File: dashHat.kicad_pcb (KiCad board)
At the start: 4 copper layers, 65 x 56 mm, 156 parts, among them J1 Input, J2 LCD, J3 GPIO, J4 LEDs, J5 Ride Through, J6 SMA, J7 Conn_01x08, Q1 BSS138, Q10 ADP197, Q12 BSS138, Q2 BSS138, Q3 2N7002, Q4 BSS84, Q5 BSS84, Q6 BSS84, Q7 , Q8 , Q9 BSS84, U1 CAT24C256, U12 MAX22193, U13 IX4427, U2 MAX17614, U3 TVS3300DRV, U4 LM61480, U5 74LVC1G80, U6 ZOE-M8Q, U7 TCAN330, U8 MCP2515-xST, U9 MAX3227, Y1 32.768k, Y2 12MHz

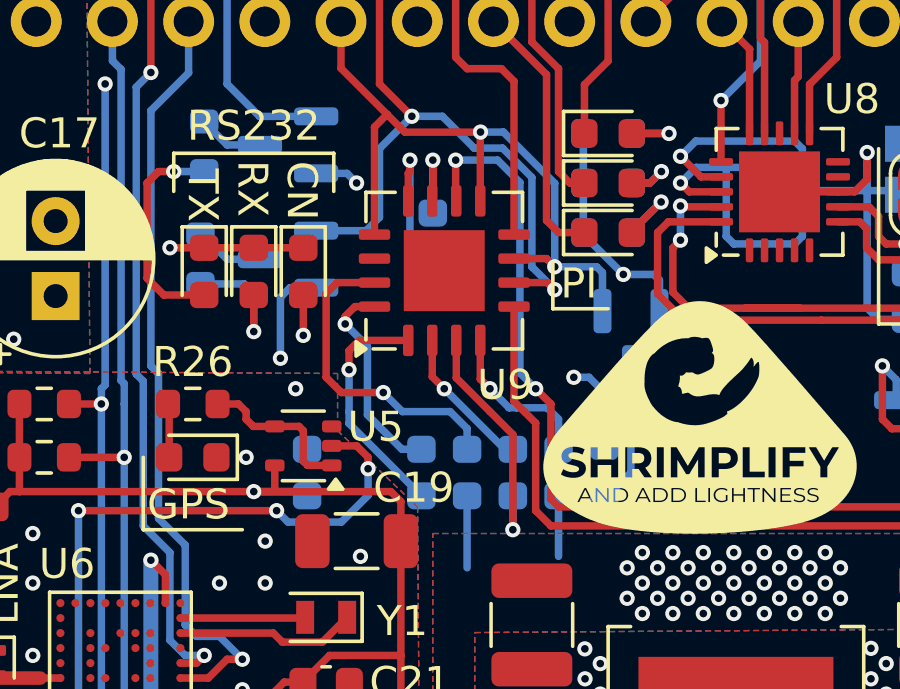
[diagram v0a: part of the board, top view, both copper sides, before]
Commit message: flip logic on rs232 conn led
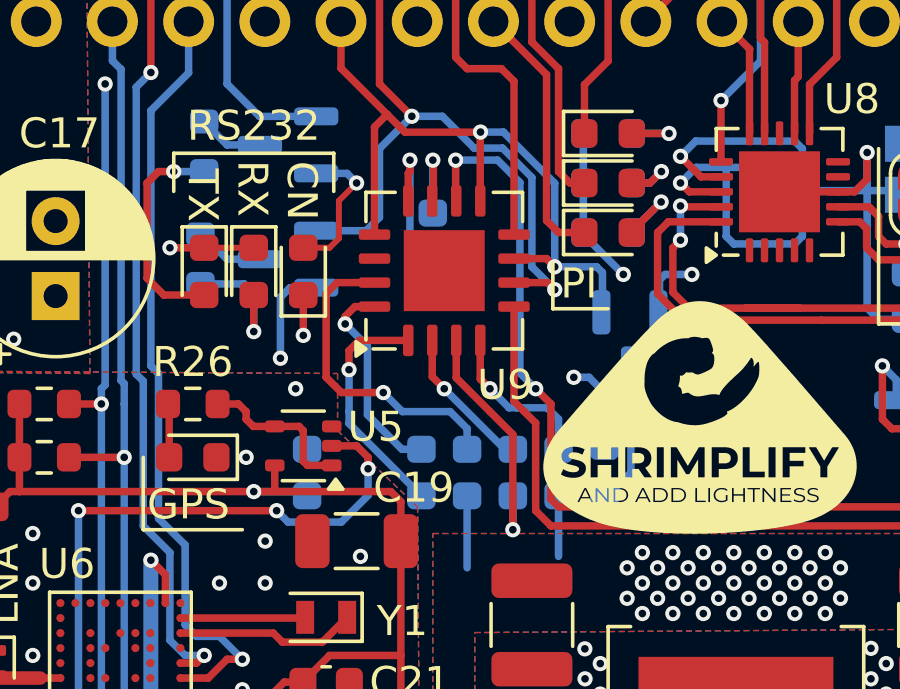
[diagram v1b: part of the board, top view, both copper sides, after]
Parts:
- Q6: value BSS84 -> 2N7002
- R1, R3: value 1.8k -> 1.5k
- R19: value 560 -> 680
- R25, R27, R28, R5, R6: value 3.9k -> 3.3k
- R26, R31, R32, R33, R34, R43, R46, R47, R7: value 220 -> 270
- moved Q6 0.05 mm to (130.7, 59.4)
- turned D13 to 90 degrees
- turned R34 to -90 degrees
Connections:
- D13 pad 1: GND -> Net-(D13-K)
- D13 pad 2: Net-(D13-A) -> +3V3
- Q6 pad 2: +3V3 -> GND
- R34 pad 1: Net-(Q6-D) -> Net-(D13-K)
- R34 pad 2: Net-(D13-A) -> Net-(Q6-D)
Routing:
- net Net-(D13-K): track 0.00 -> 15.4 mm, vias 0 -> 2
- net Net-(D13-A): track 15.4 -> 0.00 mm, vias 2 -> 0
- net +3V3: track 200.9 -> 202.0 mm
- net GND: track 101.0 -> 101.6 mm, vias 130 -> 131

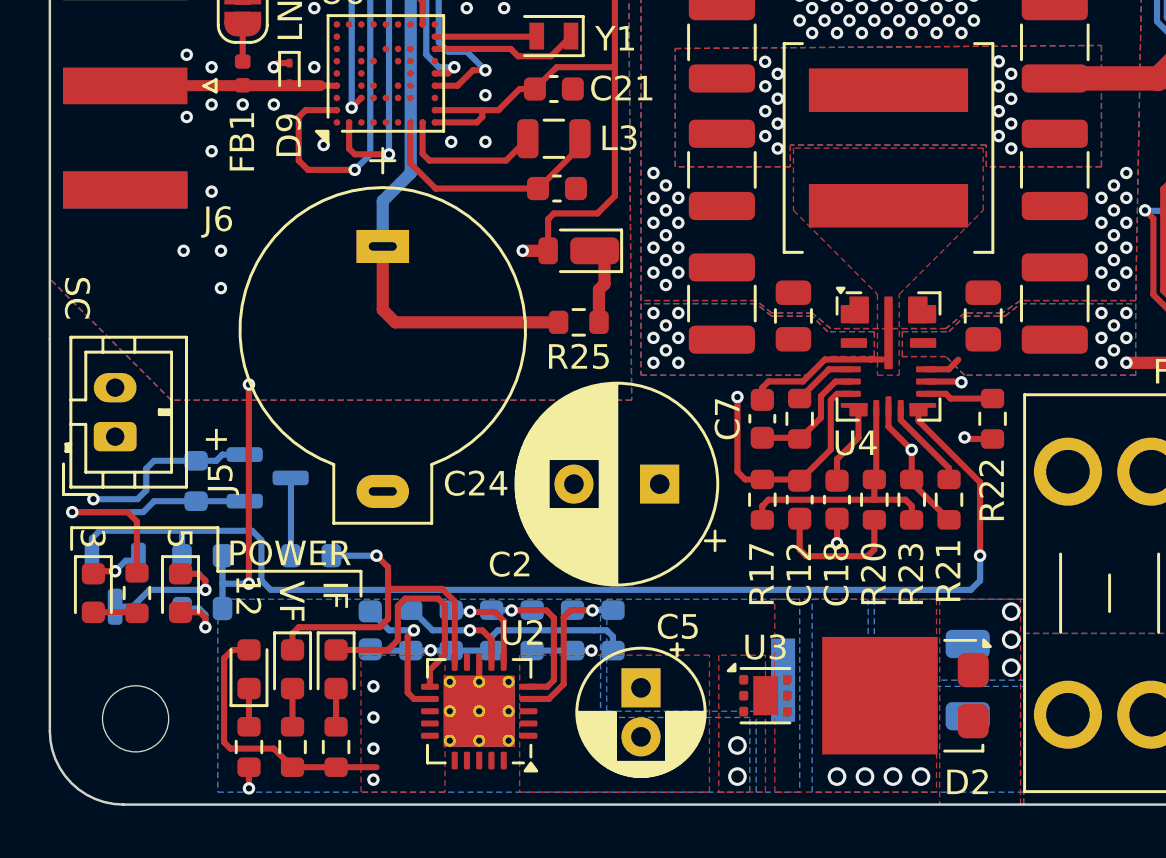
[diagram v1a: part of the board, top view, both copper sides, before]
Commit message: remove vf led, add en divider to 5v regulator to fix sequencing
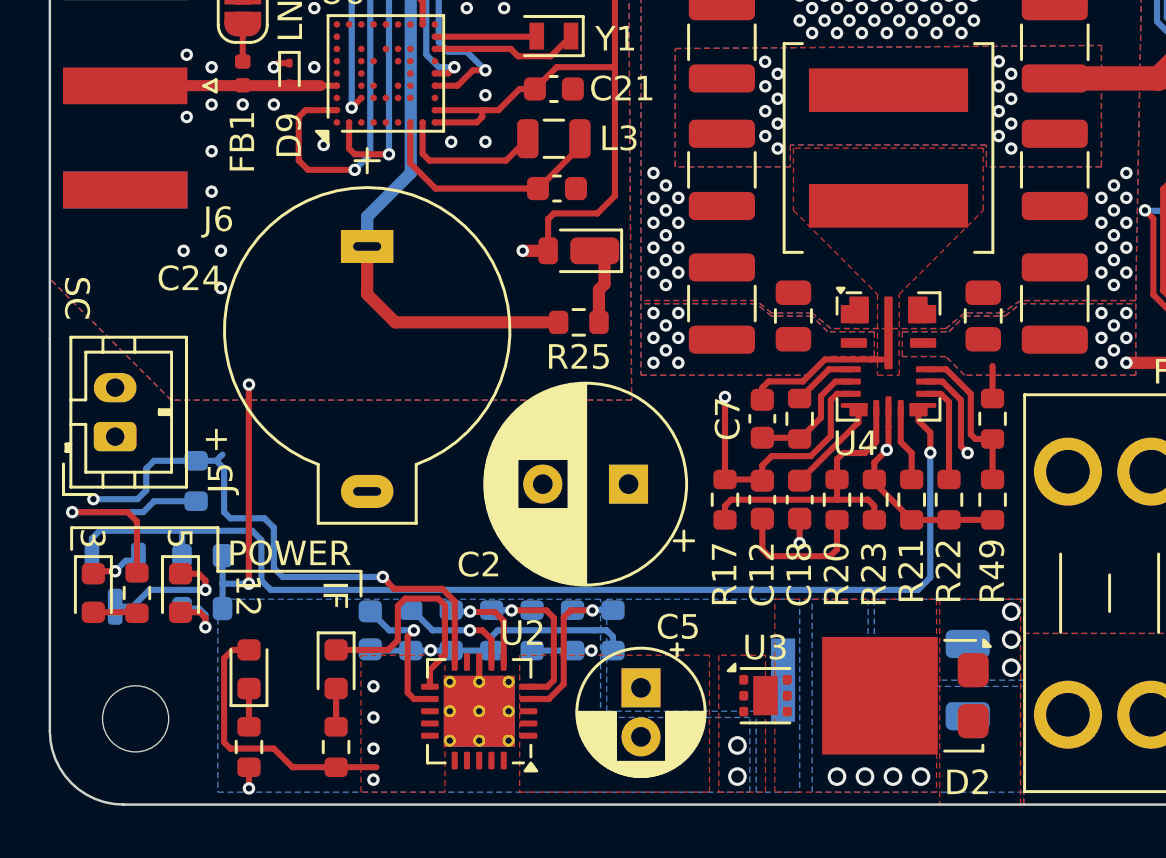
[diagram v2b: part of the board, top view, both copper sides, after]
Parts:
- removed D5: Red, LED_SMD:LED_0603_1608Metric
- removed Q12: BSS138, Package_TO_SOT_SMD:SOT-23
- R11: value 2k -> 330k
- R49: value 10k -> 100k; moved to F.Cu
- moved R11 31.6 mm to (138.5, 84.3), turned to -90 degrees
- moved R49 27.9 mm to (138.5, 87.6), turned to -90 degrees
- moved R22 3.75 mm to (136.7, 87.6)
- moved C12 1.52 mm to (129.1, 87.6)
- moved C18 1.52 mm to (130.6, 87.6)
- moved R17 1.52 mm to (127.6, 87.6)
- moved R20 1.52 mm to (132.1, 87.6)
- moved R21 1.52 mm to (135.2, 87.6)
- moved R23 1.52 mm to (133.7, 87.6)
- moved C2 1.27 mm to (123.6, 86.9)
- moved C24 0.64 mm to (113.0, 77.2)
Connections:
- R11 pad 2: Net-(D5-A) -> Net-(U4-EN)
- R49 pad 1: Net-(D5-K) -> Net-(U4-EN)
- R49 pad 2: Net-(Q12-D) -> GND
- U2 pad 10: Net-(D5-K) -> /GPIO27
- U4 pad 13: +12V -> Net-(U4-EN)
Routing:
- net /GPIO27: track 76.3 -> 92.0 mm, vias 2 -> 3
- net Net-(D5-K): track 14.9 -> 0.00 mm, vias 1 -> 0
- net Net-(U4-EN): track 0.00 -> 6.51 mm
- net GND: track 101.6 -> 106.1 mm, vias 131 -> 130
- net Net-(Q12-D): track 3.29 -> 0.00 mm
- net Net-(Q3-G): track 48.5 -> 45.5 mm
- net +3V3: track 202.0 -> 200.0 mm
- net Net-(D5-A): track 1.56 -> 0.00 mm
- net Net-(U4-SPSP): track 2.79 -> 4.23 mm
- net Net-(U4-FB): track 11.2 -> 12.5 mm
- net Net-(U4-VCC): track 3.26 -> 3.90 mm
- net Net-(U4-RT): track 3.73 -> 3.09 mm
- net Net-(U6-V_BCKP): track 22.6 -> 23.1 mm
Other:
- board text removed: "VF"
